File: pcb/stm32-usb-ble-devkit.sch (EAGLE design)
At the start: 102 parts, among them CN1 USB-MICROB-2TABS, CN2 USB-C-2.0-FEMALE, CN3 USB-C-2.0-FEMALE, Q2 AO3402, Q4 AO3401, U1 STM32F103-48LQFP, U2 STM32F205-64, U3 TUSB320, U4 TUSB320, U5 HOLYIOT-17051-NRF51822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

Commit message: pcb: Switch headers to round pads
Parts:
- JP10, JP9: device pinhead:PINHD-1X4 -> tuetuopay:PINHD-1X4
- JP7: device pinhead:PINHD-1X3 -> tuetuopay:PINHD-1X3
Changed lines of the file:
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@@
 <part name="R16" library="tuetuopay" deviceset="R" device="R0603" value="100k"/>
 <part name="GND27" library="supply1" library_urn="urn:adsk.eagle:library:371" deviceset="GND" device=""/>
-<part name="JP7" library="pinhead" library_urn="urn:adsk.eagle:library:325" deviceset="PINHD-1X3" device="" package3d_urn="urn:adsk.eagle:package:22458/2"/>
+<part name="JP7" library="tuetuopay" deviceset="PINHD-1X3" device="" package3d_urn="urn:adsk.eagle:package:22458/2"/>
 <part name="P+1" library="supply1" library_urn="urn:adsk.eagle:library:371" deviceset="+5V" device=""/>
 <part name="LED3" library="led" library_urn="urn:adsk.eagle:library:259" deviceset="LED" device="CHIP-LED0603" package3d_urn="urn:adsk.eagle:package:15819/3"/>
@@
 <part name="+3V24" library="supply1" library_urn="urn:adsk.eagle:library:371" deviceset="+3V3" device=""/>
 <part name="P+6" library="supply1" library_urn="urn:adsk.eagle:library:371" deviceset="+5V" device=""/>
-<part name="JP9" library="pinhead" library_urn="urn:adsk.eagle:library:325" deviceset="PINHD-1X4" device="" package3d_urn="urn:adsk.eagle:package:22407/2"/>
-<part name="JP10" library="pinhead" library_urn="urn:adsk.eagle:library:325" deviceset="PINHD-1X4" device="" package3d_urn="urn:adsk.eagle:package:22407/2"/>
+<part name="JP9" library="tuetuopay" deviceset="PINHD-1X4" device="" package3d_urn="urn:adsk.eagle:package:22407/2"/>
+<part name="JP10" library="tuetuopay" deviceset="PINHD-1X4" device="" package3d_urn="urn:adsk.eagle:package:22407/2"/>
 <part name="JP11" library="pinhead" library_urn="urn:adsk.eagle:library:325" deviceset="PINHD-2X3" device="" package3d_urn="urn:adsk.eagle:package:22462/2"/>
 <part name="JP12" library="pinhead" library_urn="urn:adsk.eagle:library:325" deviceset="PINHD-2X3" device="" package3d_urn="urn:adsk.eagle:package:22462/2"/>

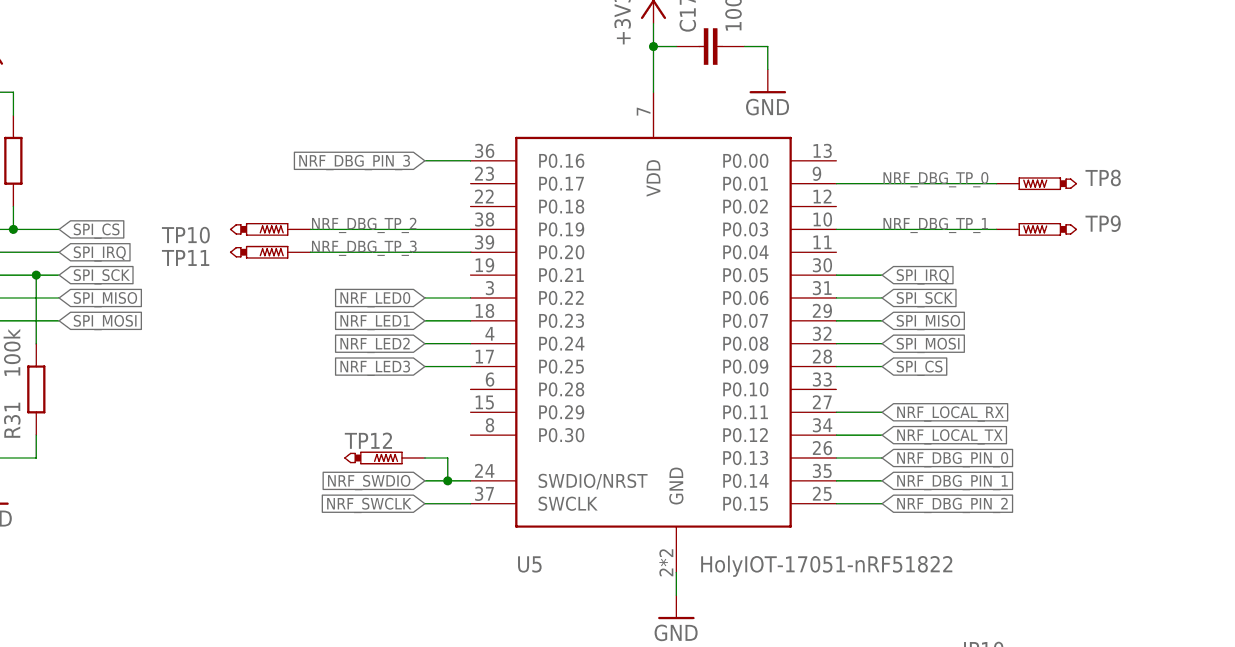
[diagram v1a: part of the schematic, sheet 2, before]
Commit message: pcb: Moved all nRF TP to the same side
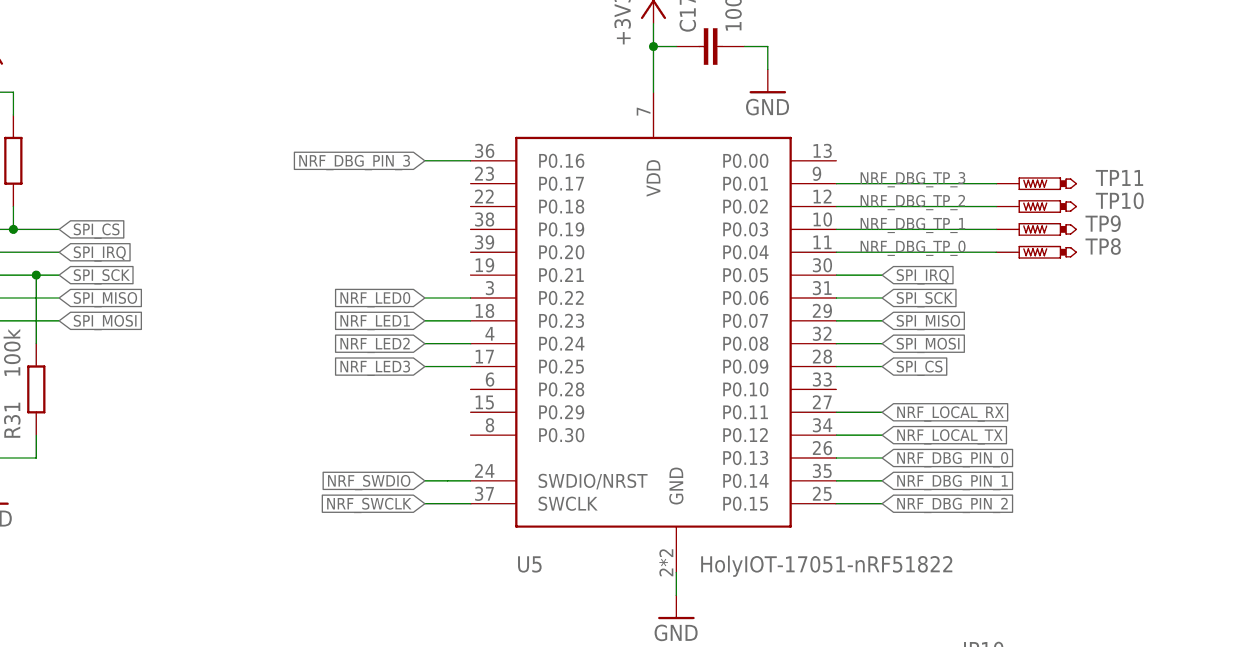
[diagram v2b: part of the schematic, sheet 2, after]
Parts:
- removed TP12: PTR1B1,27, testpad:PTR1B1,27
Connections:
- net NRF_DBG_TP_0: now also U5.P0.04; no longer U5.P0.01
- net NRF_DBG_TP_2: now also U5.P0.02; no longer U5.P0.19
- net NRF_DBG_TP_3: now also U5.P0.01; no longer U5.P0.20
- net NRF_SWDIO: no longer TP12.TP
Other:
- moved on the sheet: TP10, TP11, TP8
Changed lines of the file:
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@@
 <part name="TP10" library="testpad" library_urn="urn:adsk.eagle:library:385" deviceset="PTR1" device="B1,27" package3d_urn="urn:adsk.eagle:package:27944/1"/>
 <part name="TP11" library="testpad" library_urn="urn:adsk.eagle:library:385" deviceset="PTR1" device="B1,27" package3d_urn="urn:adsk.eagle:package:27944/1"/>
-<part name="TP12" library="testpad" library_urn="urn:adsk.eagle:library:385" deviceset="PTR1" device="B1,27" package3d_urn="urn:adsk.eagle:package:27944/1"/>
 <part name="JP8" library="pinhead" library_urn="urn:adsk.eagle:library:325" deviceset="PINHD-2X3" device="" package3d_urn="urn:adsk.eagle:package:22462/2"/>
 <part name="LED7" library="led" library_urn="urn:adsk.eagle:library:259" deviceset="LED" device="CHIP-LED0603" package3d_urn="urn:adsk.eagle:package:15819/3"/>
@@
 <instance part="C17" gate="&gt;NAME" x="205.74" y="165.1" rot="R90"/>
 <instance part="GND32" gate="1" x="213.36" y="160.02"/>
-<instance part="TP8" gate="G$1" x="241.3" y="149.86" smashed="yes" rot="R90">
-<attribute name="NAME" x="252.73" y="151.384" size="1.778" layer="95" rot="R180"/>
-<attribute name="TP_SIGNAL_NAME" x="243.84" y="151.13" size="1.778" layer="97" rot="R90"/>
+<instance part="TP8" gate="G$1" x="241.3" y="142.24" smashed="yes" rot="R90">
+<attribute name="NAME" x="252.73" y="143.764" size="1.778" layer="95" rot="R180"/>
+<attribute name="TP_SIGNAL_NAME" x="243.84" y="143.51" size="1.778" layer="97" rot="R90"/>
 </instance>
 <instance part="TP9" gate="G$1" x="241.3" y="144.78" smashed="yes" rot="R90">
@@
 <attribute name="TP_SIGNAL_NAME" x="243.84" y="146.05" size="1.778" layer="97" rot="R90"/>
 </instance>
-<instance part="TP10" gate="G$1" x="160.02" y="144.78" smashed="yes" rot="R270">
-<attribute name="NAME" x="146.05" y="143.256" size="1.778" layer="95"/>
-<attribute name="TP_SIGNAL_NAME" x="157.48" y="143.51" size="1.778" layer="97" rot="R270"/>
-</instance>
-<instance part="TP11" gate="G$1" x="160.02" y="142.24" smashed="yes" rot="R270">
-<attribute name="NAME" x="146.05" y="140.716" size="1.778" layer="95"/>
-<attribute name="TP_SIGNAL_NAME" x="157.48" y="140.97" size="1.778" layer="97" rot="R270"/>
-</instance>
-<instance part="TP12" gate="G$1" x="172.72" y="119.38" smashed="yes" rot="R270">
-<attribute name="NAME" x="166.37" y="120.396" size="1.778" layer="95"/>
-<attribute name="TP_SIGNAL_NAME" x="170.18" y="118.11" size="1.778" layer="97" rot="R270"/>
+<instance part="TP10" gate="G$1" x="241.3" y="147.32" smashed="yes" rot="R90">
+<attribute name="NAME" x="255.27" y="148.844" size="1.778" layer="95" rot="R180"/>
+<attribute name="TP_SIGNAL_NAME" x="243.84" y="148.59" size="1.778" layer="97" rot="R90"/>
+</instance>
+<instance part="TP11" gate="G$1" x="241.3" y="149.86" smashed="yes" rot="R90">
+<attribute name="NAME" x="255.27" y="151.384" size="1.778" layer="95" rot="R180"/>
+<attribute name="TP_SIGNAL_NAME" x="243.84" y="151.13" size="1.778" layer="97" rot="R90"/>
 </instance>
 <instance part="JP8" gate="A" x="152.4" y="88.9"/>
@@
 <wire x1="180.34" y1="116.84" x2="177.8" y2="116.84" width="0.1524" layer="91"/>
 <label x="175.26" y="116.84" size="1.27" layer="95" rot="R180" xref="yes"/>
-<pinref part="TP12" gate="G$1" pin="TP"/>
 <wire x1="177.8" y1="116.84" x2="175.26" y2="116.84" width="0.1524" layer="91"/>
-<wire x1="175.26" y1="119.38" x2="177.8" y2="119.38" width="0.1524" layer="91"/>
-<wire x1="177.8" y1="119.38" x2="177.8" y2="116.84" width="0.1524" layer="91"/>
-<junction x="177.8" y="116.84"/>
 </segment>
 </net>
@@
 </segment>
 </net>
-<net name="NRF_DBG_TP_2" class="0">
-<segment>
-<pinref part="U5" gate="G$1" pin="P0.19"/>
-<wire x1="180.34" y1="144.78" x2="162.56" y2="144.78" width="0.1524" layer="91"/>
-<pinref part="TP10" gate="G$1" pin="TP"/>
-<label x="162.56" y="144.78" size="1.27" layer="95"/>
-</segment>
-</net>
-<net name="NRF_DBG_TP_3" class="0">
-<segment>
-<pinref part="U5" gate="G$1" pin="P0.20"/>
-<wire x1="180.34" y1="142.24" x2="162.56" y2="142.24" width="0.1524" layer="91"/>
-<pinref part="TP11" gate="G$1" pin="TP"/>
-<label x="162.56" y="142.24" size="1.27" layer="95"/>
-</segment>
-</net>
-<net name="NRF_DBG_TP_0" class="0">
-<segment>
-<pinref part="U5" gate="G$1" pin="P0.01"/>
-<wire x1="220.98" y1="149.86" x2="238.76" y2="149.86" width="0.1524" layer="91"/>
-<pinref part="TP8" gate="G$1" pin="TP"/>
-<label x="226.06" y="149.86" size="1.27" layer="95"/>
-</segment>
-</net>
 <net name="NRF_DBG_TP_1" class="0">
 <segment>
@@
 <wire x1="220.98" y1="144.78" x2="238.76" y2="144.78" width="0.1524" layer="91"/>
 <pinref part="TP9" gate="G$1" pin="TP"/>
-<label x="226.06" y="144.78" size="1.27" layer="95"/>
+<label x="223.52" y="144.78" size="1.27" layer="95"/>
 </segment>
 </net>
@@
 </segment>
 </net>
+<net name="NRF_DBG_TP_0" class="0">
+<segment>
+<pinref part="TP8" gate="G$1" pin="TP"/>
+<pinref part="U5" gate="G$1" pin="P0.04"/>
+<wire x1="238.76" y1="142.24" x2="220.98" y2="142.24" width="0.1524" layer="91"/>
+<label x="223.52" y="142.24" size="1.27" layer="95"/>
+</segment>
+</net>
+<net name="NRF_DBG_TP_2" class="0">
+<segment>
+<pinref part="TP10" gate="G$1" pin="TP"/>
+<pinref part="U5" gate="G$1" pin="P0.02"/>
+<wire x1="238.76" y1="147.32" x2="220.98" y2="147.32" width="0.1524" layer="91"/>
+<label x="223.52" y="147.32" size="1.27" layer="95"/>
+</segment>
+</net>
+<net name="NRF_DBG_TP_3" class="0">
+<segment>
+<pinref part="TP11" gate="G$1" pin="TP"/>
+<pinref part="U5" gate="G$1" pin="P0.01"/>
+<wire x1="238.76" y1="149.86" x2="220.98" y2="149.86" width="0.1524" layer="91"/>
+<label x="223.52" y="149.86" size="1.27" layer="95"/>
+</segment>
+</net>

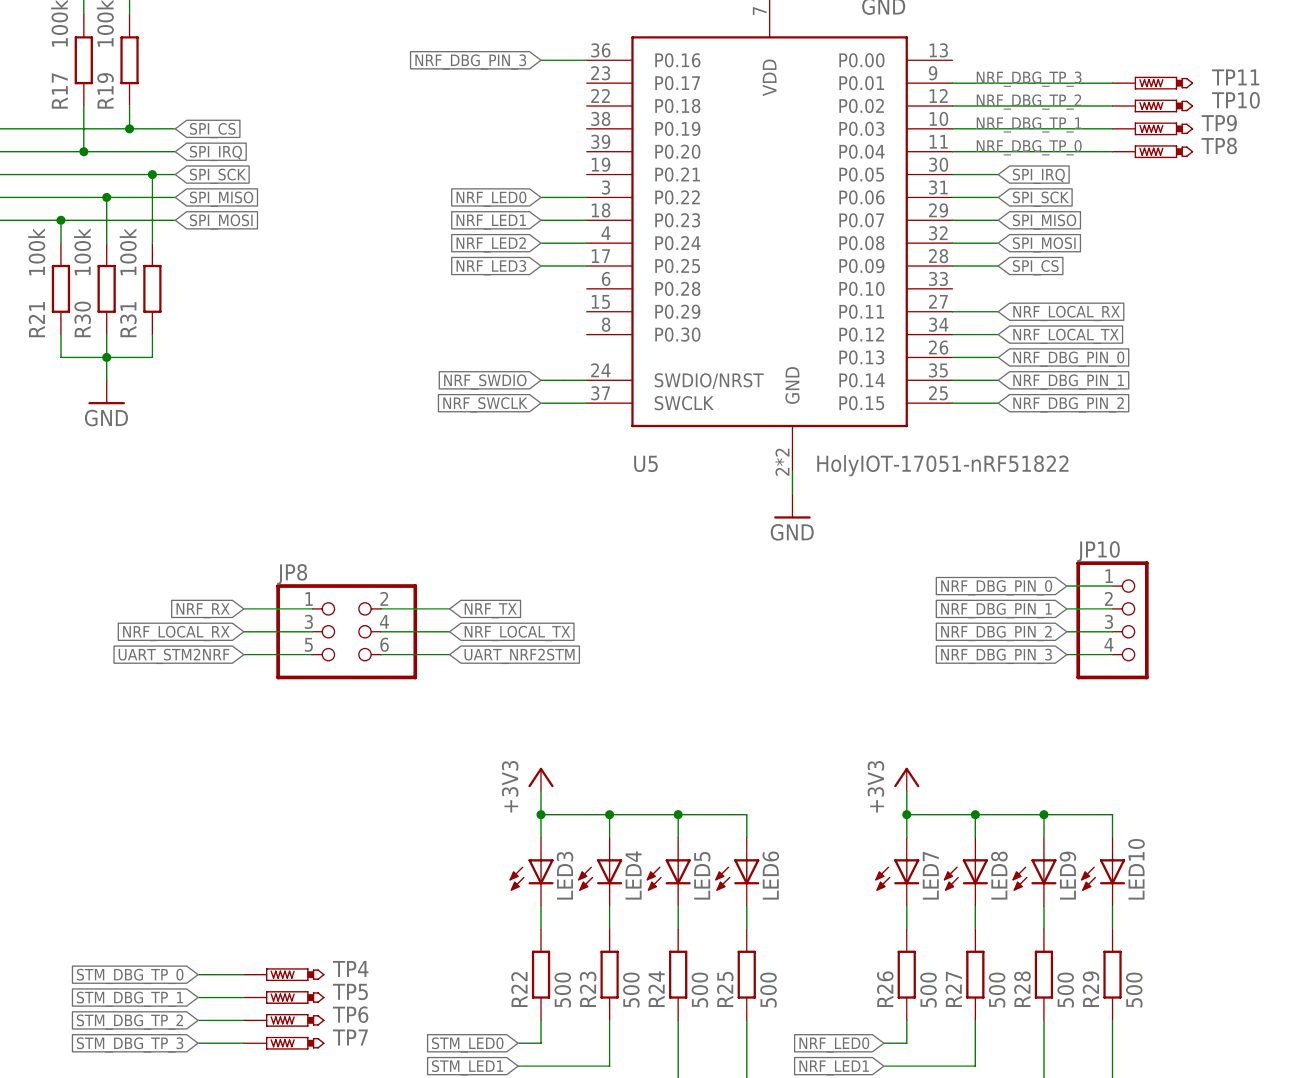
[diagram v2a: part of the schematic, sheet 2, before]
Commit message: pcb: Add SPI header
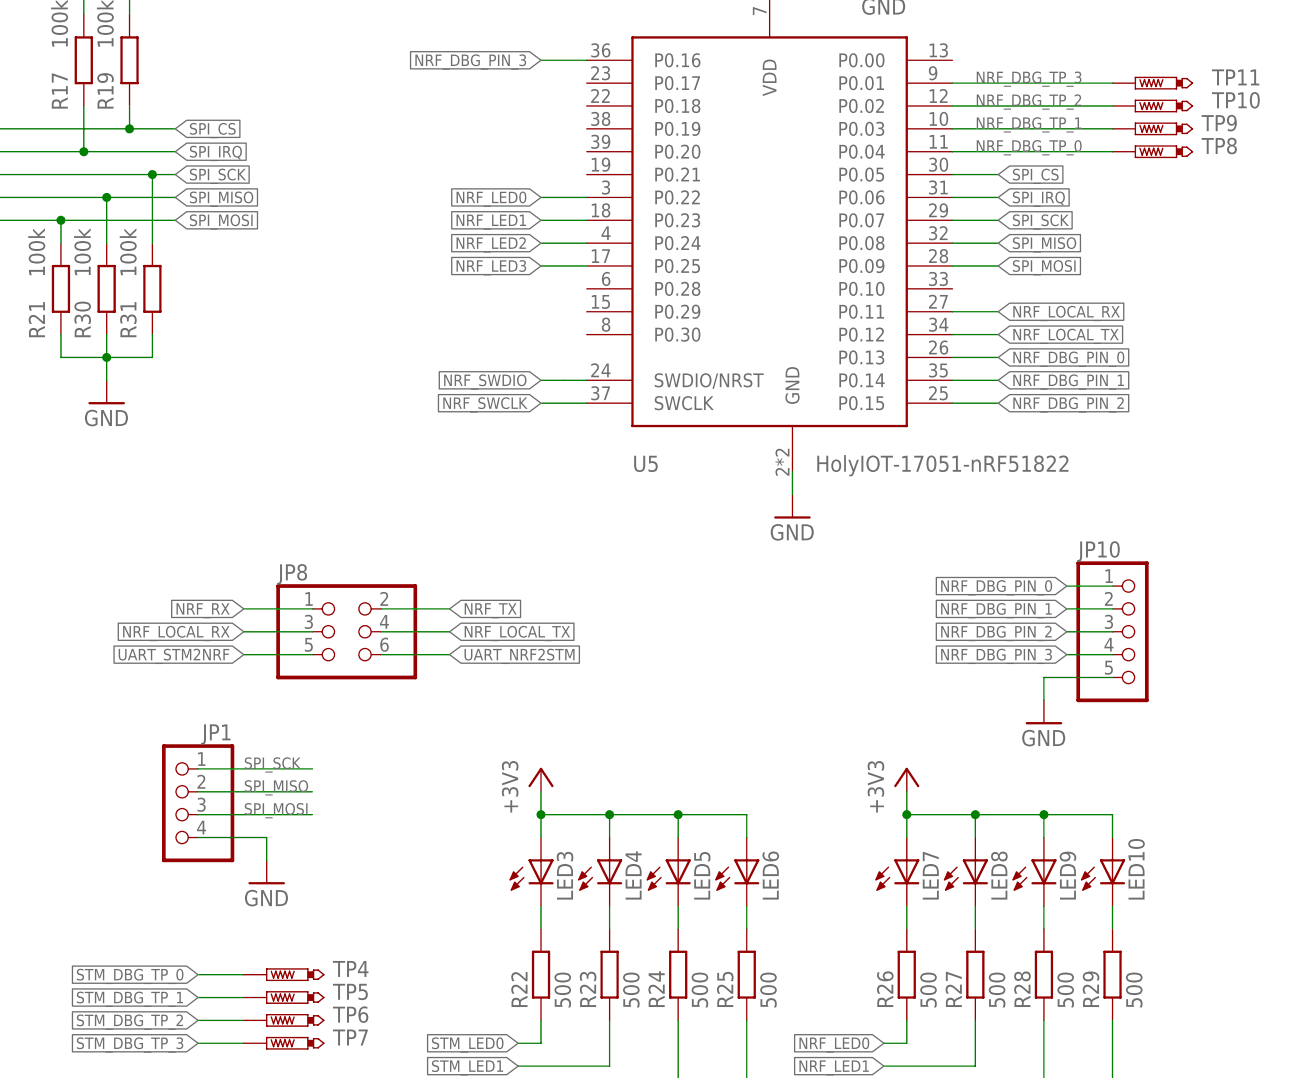
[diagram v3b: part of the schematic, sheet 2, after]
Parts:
- added JP1: (no value), tuetuopay:PINHD-1X4
- JP10: device tuetuopay:PINHD-1X4 -> tuetuopay:PINHD-1X5
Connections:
- net GND: now also JP1.4, JP10.5
- net SPI_CS: now also U5.P0.05; no longer U5.P0.09
- net SPI_IRQ: now also U5.P0.06; no longer U5.P0.05
- net SPI_MISO: now also JP1.2, U5.P0.08; no longer U5.P0.07
- net SPI_MOSI: now also JP1.3, U5.P0.09; no longer U5.P0.08
- net SPI_SCK: now also JP1.1, U5.P0.07; no longer U5.P0.06
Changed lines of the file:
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@@
 <part name="P+6" library="supply1" library_urn="urn:adsk.eagle:library:371" deviceset="+5V" device=""/>
 <part name="JP9" library="tuetuopay" deviceset="PINHD-1X4" device="" package3d_urn="urn:adsk.eagle:package:22407/2"/>
-<part name="JP10" library="tuetuopay" deviceset="PINHD-1X4" device="" package3d_urn="urn:adsk.eagle:package:22407/2"/>
+<part name="JP10" library="tuetuopay" deviceset="PINHD-1X5" device="" package3d_urn="urn:adsk.eagle:package:22469/2"/>
 <part name="JP11" library="pinhead" library_urn="urn:adsk.eagle:library:325" deviceset="PINHD-2X3" device="" package3d_urn="urn:adsk.eagle:package:22462/2"/>
 <part name="JP12" library="pinhead" library_urn="urn:adsk.eagle:library:325" deviceset="PINHD-2X3" device="" package3d_urn="urn:adsk.eagle:package:22462/2"/>
@@
 <part name="R33" library="tuetuopay" deviceset="R" device="R0603" value="68k"/>
 <part name="C23" library="tuetuopay" deviceset="C" device="0603" value="10u"/>
+<part name="GND30" library="supply1" library_urn="urn:adsk.eagle:library:371" deviceset="GND" device=""/>
+<part name="JP1" library="tuetuopay" deviceset="PINHD-1X4" device="" package3d_urn="urn:adsk.eagle:package:22407/2"/>
+<part name="GND34" library="supply1" library_urn="urn:adsk.eagle:library:371" deviceset="GND" device=""/>
 </parts>
 <sheets>
@@
 <instance part="+3V19" gate="G$1" x="127" y="165.1"/>
 <instance part="GND28" gate="1" x="127" y="114.3"/>
+<instance part="GND30" gate="1" x="231.14" y="78.74"/>
+<instance part="JP1" gate="A" x="134.62" y="68.58" rot="MR0"/>
+<instance part="GND34" gate="1" x="144.78" y="60.96"/>
 </instances>
 <busses>
@@
 <wire x1="127" y1="116.84" x2="127" y2="119.38" width="0.1524" layer="91"/>
 </segment>
+<segment>
+<pinref part="GND30" gate="1" pin="GND"/>
+<pinref part="JP10" gate="A" pin="5"/>
+<wire x1="231.14" y1="81.28" x2="231.14" y2="83.82" width="0.1524" layer="91"/>
+<wire x1="231.14" y1="83.82" x2="238.76" y2="83.82" width="0.1524" layer="91"/>
+</segment>
+<segment>
+<pinref part="JP1" gate="A" pin="4"/>
+<pinref part="GND34" gate="1" pin="GND"/>
+<wire x1="137.16" y1="66.04" x2="144.78" y2="66.04" width="0.1524" layer="91"/>
+<wire x1="144.78" y1="66.04" x2="144.78" y2="63.5" width="0.1524" layer="91"/>
+</segment>
 </net>
 <net name="+3V3" class="0">
@@
 </segment>
 <segment>
-<label x="226.06" y="137.16" size="1.27" layer="95" xref="yes"/>
-<pinref part="U5" gate="G$1" pin="P0.06"/>
-<wire x1="220.98" y1="137.16" x2="226.06" y2="137.16" width="0.1524" layer="91"/>
+<label x="226.06" y="134.62" size="1.27" layer="95" xref="yes"/>
+<pinref part="U5" gate="G$1" pin="P0.07"/>
+<wire x1="220.98" y1="134.62" x2="226.06" y2="134.62" width="0.1524" layer="91"/>
+</segment>
+<segment>
+<pinref part="JP1" gate="A" pin="1"/>
+<wire x1="137.16" y1="73.66" x2="149.86" y2="73.66" width="0.1524" layer="91"/>
+<label x="142.24" y="73.66" size="1.27" layer="95"/>
 </segment>
 </net>
@@
 </segment>
 <segment>
-<label x="226.06" y="134.62" size="1.27" layer="95" xref="yes"/>
-<pinref part="U5" gate="G$1" pin="P0.07"/>
-<wire x1="220.98" y1="134.62" x2="226.06" y2="134.62" width="0.1524" layer="91"/>
+<label x="226.06" y="132.08" size="1.27" layer="95" xref="yes"/>
+<pinref part="U5" gate="G$1" pin="P0.08"/>
+<wire x1="220.98" y1="132.08" x2="226.06" y2="132.08" width="0.1524" layer="91"/>
+</segment>
+<segment>
+<pinref part="JP1" gate="A" pin="2"/>
+<wire x1="137.16" y1="71.12" x2="149.86" y2="71.12" width="0.1524" layer="91"/>
+<label x="142.24" y="71.12" size="1.27" layer="95"/>
 </segment>
 </net>
@@
 </segment>
 <segment>
-<label x="226.06" y="132.08" size="1.27" layer="95" xref="yes"/>
-<pinref part="U5" gate="G$1" pin="P0.08"/>
-<wire x1="220.98" y1="132.08" x2="226.06" y2="132.08" width="0.1524" layer="91"/>
+<pinref part="U5" gate="G$1" pin="P0.09"/>
+<wire x1="220.98" y1="129.54" x2="226.06" y2="129.54" width="0.1524" layer="91"/>
+<label x="226.06" y="129.54" size="1.27" layer="95" xref="yes"/>
+</segment>
+<segment>
+<pinref part="JP1" gate="A" pin="3"/>
+<wire x1="137.16" y1="68.58" x2="149.86" y2="68.58" width="0.1524" layer="91"/>
+<label x="142.24" y="68.58" size="1.27" layer="95"/>
 </segment>
 </net>
@@
 </segment>
 <segment>
-<label x="226.06" y="139.7" size="1.27" layer="95" xref="yes"/>
-<pinref part="U5" gate="G$1" pin="P0.05"/>
-<wire x1="220.98" y1="139.7" x2="226.06" y2="139.7" width="0.1524" layer="91"/>
+<label x="226.06" y="137.16" size="1.27" layer="95" xref="yes"/>
+<pinref part="U5" gate="G$1" pin="P0.06"/>
+<wire x1="220.98" y1="137.16" x2="226.06" y2="137.16" width="0.1524" layer="91"/>
 </segment>
 </net>
@@
 </segment>
 <segment>
-<pinref part="U5" gate="G$1" pin="P0.09"/>
-<wire x1="220.98" y1="129.54" x2="226.06" y2="129.54" width="0.1524" layer="91"/>
-<label x="226.06" y="129.54" size="1.27" layer="95" xref="yes"/>
-</segment>
-</net>
+<label x="226.06" y="139.7" size="1.27" layer="95" xref="yes"/>
+<pinref part="U5" gate="G$1" pin="P0.05"/>
+<wire x1="220.98" y1="139.7" x2="226.06" y2="139.7" width="0.1524" layer="91"/>
+</segment>
+</net>
